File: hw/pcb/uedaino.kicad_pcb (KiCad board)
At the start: 2 copper layers, 6 parts, among them IC1 ATMEGA328P-A, SW1 SW_PUSH

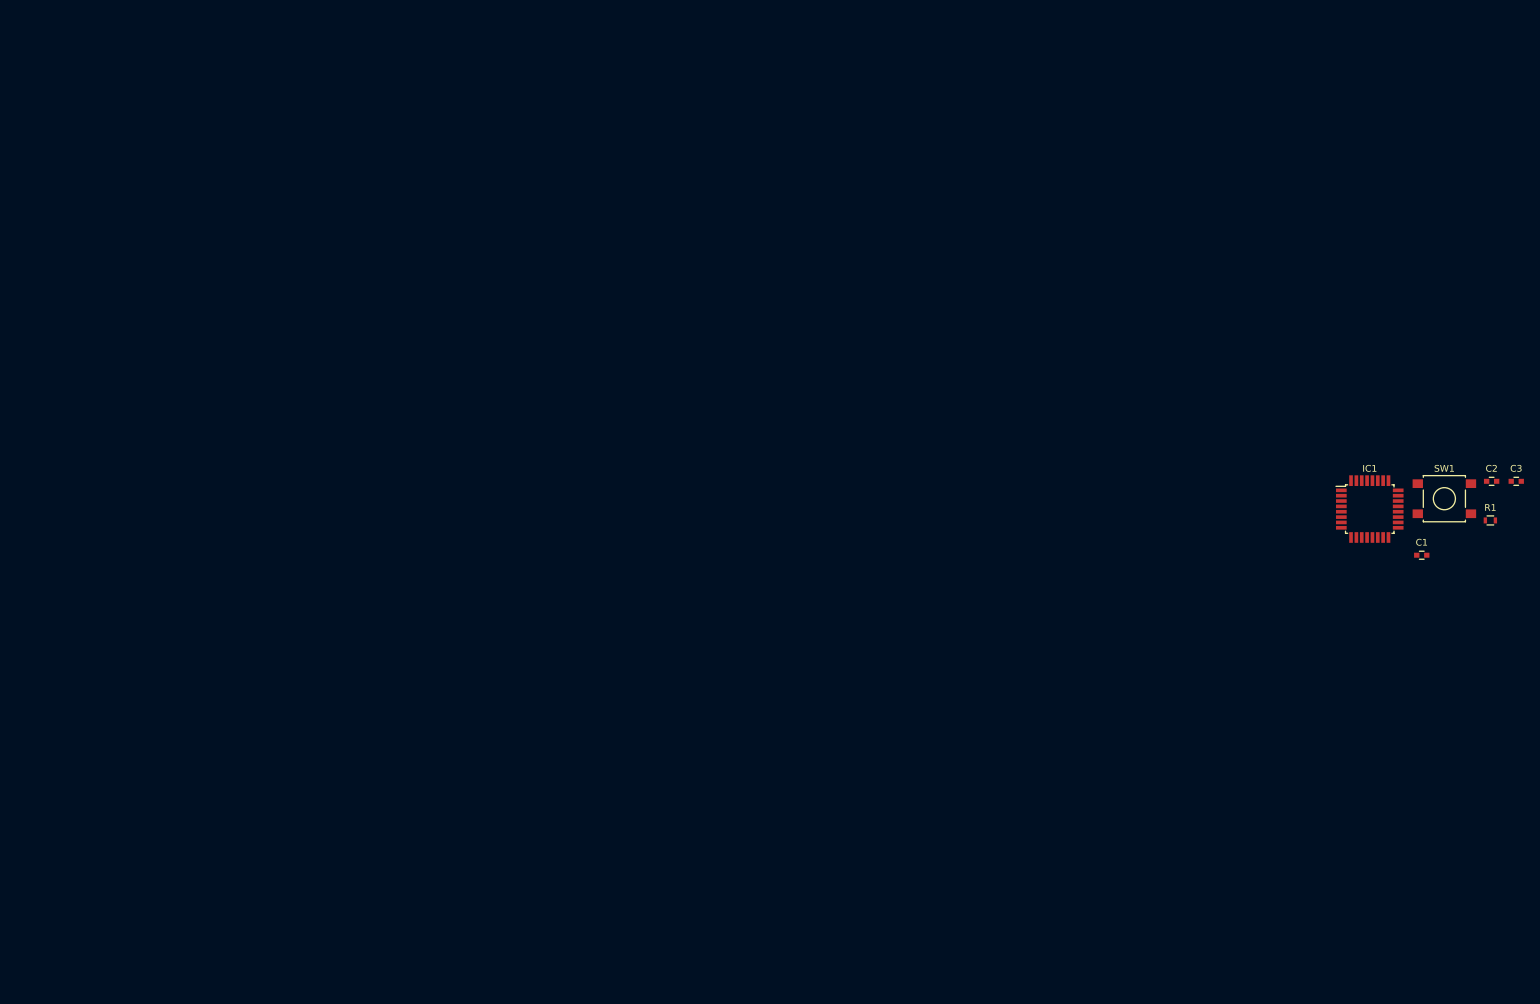
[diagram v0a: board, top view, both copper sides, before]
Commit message: Add functions
Add power circuit.
Add Capacitive Touch Sensor circuit.
Add pin header.
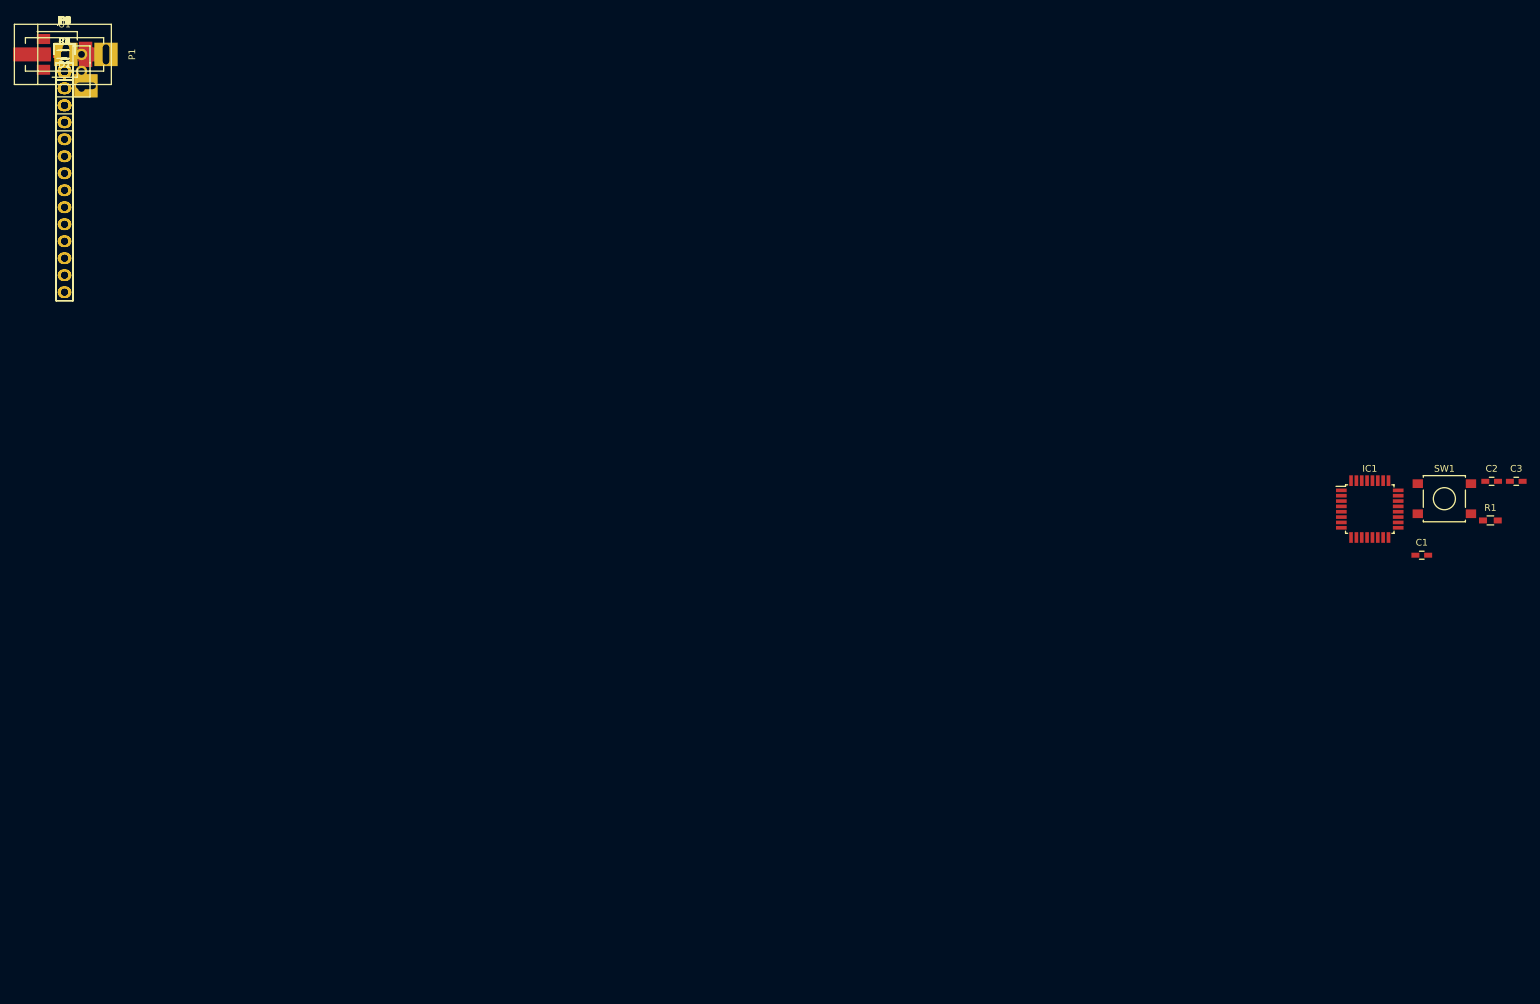
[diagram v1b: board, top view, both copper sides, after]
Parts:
- added C4, C5: 10uF, Capacitors_SMD:C_0603_HandSoldering, F.Cu at (0.00, 0.00)
- added C6, C7: 22uF, Capacitors_SMD:C_0603_HandSoldering, F.Cu at (0.00, 0.00)
- added D1: LED_+5V, Diodes_SMD:D_0603, F.Cu at (0.00, 0.00)
- added D2: LED_+3V3, Diodes_SMD:D_0603, F.Cu at (0.00, 0.00)
- added JP1, JP2, JP3, JP4, JP5, JP6, JP7, JP8, JP9: Jumper_NC_Small, Pin_Headers:Pin_Header_Straight_1x02, F.Cu at (0.00, 0.00)
- added P1: CN_PWR, Connect:BARREL_JACK, F.Cu at (0.00, 0.00)
- added P2: CN_UART, Pin_Headers:Pin_Header_Straight_1x05, F.Cu at (0.00, 0.00)
- added P3: CN_HEADER1, Pin_Headers:Pin_Header_Straight_1x15, F.Cu at (0.00, 0.00)
- added P4: CN_I2C, Pin_Headers:Pin_Header_Straight_1x04, F.Cu at (0.00, 0.00)
- added P5: CN_HEADER2, Pin_Headers:Pin_Header_Straight_1x15, F.Cu at (0.00, 0.00)
- added P6: CN_ICSP, Pin_Headers:Pin_Header_Straight_2x03, F.Cu at (0.00, 0.00)
- added R2: 10M, Resistors_SMD:R_0603_HandSoldering, F.Cu at (0.00, 0.00)
- added R3, R4: 1K, Resistors_SMD:R_0603_HandSoldering, F.Cu at (0.00, 0.00)
- added R5, R6: 4.7K, Resistors_SMD:R_0603_HandSoldering, F.Cu at (0.00, 0.00)
- added U1: AP1117, TO_SOT_Packages_SMD:SOT-223, F.Cu at (0.00, 0.00)
- added Y1: 16MHz, Crystals:Crystal_HC49-SD_SMD, F.Cu at (0.00, 0.00)
- C1, C2, C3: footprint Capacitors_SMD:C_0603 -> Capacitors_SMD:C_0603_HandSoldering
- R1: footprint Resistors_SMD:R_0603 -> Resistors_SMD:R_0603_HandSoldering
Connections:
- C3 pad 1: (no net) -> /DTR
- IC1 pad 1: (no net) -> /D3
- IC1 pad 10: (no net) -> /D6
- IC1 pad 11: (no net) -> /D7
- IC1 pad 12: (no net) -> /D8
- IC1 pad 13: (no net) -> /D9
- IC1 pad 14: (no net) -> /D10
- IC1 pad 15: (no net) -> /D11
- IC1 pad 16: (no net) -> /D12
- IC1 pad 17: (no net) -> /D13
- IC1 pad 19: (no net) -> /A6
- IC1 pad 2: (no net) -> /D4
- IC1 pad 22: (no net) -> /A7
- IC1 pad 23: (no net) -> /A0
- IC1 pad 24: (no net) -> /A1
- IC1 pad 25: (no net) -> /A2
- IC1 pad 26: (no net) -> /A3
- IC1 pad 27: (no net) -> /A4/SDA
- IC1 pad 28: (no net) -> /A5/SCL
- IC1 pad 30: (no net) -> /RXD
- IC1 pad 31: (no net) -> /TXD
- IC1 pad 32: (no net) -> /D2
- IC1 pad 7: (no net) -> /XT1
- IC1 pad 8: (no net) -> /XT2
- IC1 pad 9: (no net) -> /D5
- R1 pad 1: (no net) -> +5V

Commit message: Add PCB Design
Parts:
- removed D2: LED_+3V3, Diodes_SMD:D_0603
- removed JP7, JP8, JP9: Jumper_NC_Small, Pin_Headers:Pin_Header_Straight_1x02
- removed R6: 4.7K, Resistors_SMD:R_0603_HandSoldering
- added U2: WS2812B, UeduinoLib:WS2812B, F.Cu at (154.6, 93.3)
- C3: value 0.1u -> 22uF
- C4: value 10uF -> 22uF
- C6: value 22uF -> 10uF
- C7: value 22uF -> 0.1u
- JP1: value Jumper_NC_Small -> J_CAP1; footprint Pin_Headers:Pin_Header_Straight_1x02 -> UeduinoLib:JP_CAP
- JP2: value Jumper_NC_Small -> J_CAP2; footprint Pin_Headers:Pin_Header_Straight_1x02 -> UeduinoLib:JP_CAP
- JP3: value Jumper_NC_Small -> J_CAP3; footprint Pin_Headers:Pin_Header_Straight_1x02 -> UeduinoLib:JP_CAP
- JP4: value Jumper_NC_Small -> J_CAP4; footprint Pin_Headers:Pin_Header_Straight_1x02 -> UeduinoLib:JP_CAP
- JP5: value Jumper_NC_Small -> J_CAP5; footprint Pin_Headers:Pin_Header_Straight_1x02 -> UeduinoLib:JP_CAP
- JP6: value Jumper_NC_Small -> J_CAP6; footprint Pin_Headers:Pin_Header_Straight_1x02 -> UeduinoLib:JP_CAP
- P1: value CN_PWR -> USB_OTG; footprint Connect:BARREL_JACK -> Connectors:USB_Micro-B_10103594-0001LF
- P2: value CN_UART -> CN_POWER; footprint Pin_Headers:Pin_Header_Straight_1x05 -> Socket_Strips:Socket_Strip_Straight_1x08
- P3: value CN_HEADER1 -> CN_J1; footprint Pin_Headers:Pin_Header_Straight_1x15 -> Socket_Strips:Socket_Strip_Straight_1x06
- P4: value CN_I2C -> CN_ICSP; footprint Pin_Headers:Pin_Header_Straight_1x04 -> Socket_Strips:Socket_Strip_Straight_2x03
- P5: value CN_HEADER2 -> CONN_01X10; footprint Pin_Headers:Pin_Header_Straight_1x15 -> Socket_Strips:Socket_Strip_Straight_1x10
- P6: value CN_ICSP -> CONN_01X08; footprint Pin_Headers:Pin_Header_Straight_2x03 -> Socket_Strips:Socket_Strip_Straight_1x08
- R1: value 10K -> 1K
- R2: value 10M -> 10K
- R3: value 1K -> 10M
- R4: value 1K -> 3.3K
- R5: value 4.7K -> 3.3K
- Y1: footprint Crystals:Crystal_HC49-SD_SMD -> Crystals:Crystal_SMD_5032_2Pads
- moved P6 192.8 mm to (161.3, 105.6), turned to 270 degrees
- moved JP6 191.6 mm to (149.8, 119.6)
- moved JP3 185.0 mm to (149.8, 108.6)
- moved JP5 182.6 mm to (138.0, 119.6)
- moved P5 179.6 mm to (161.3, 79.0), turned to 270 degrees
- moved C4 176.8 mm to (145.6, 100.3), turned to 270 degrees
- moved JP2 175.8 mm to (138.1, 108.7)
- moved P4 173.8 mm to (151.4, 85.2)
- moved JP4 172.9 mm to (125.7, 118.7)
- moved Y1 172.3 mm to (140.0, 100.5), turned to 180 degrees
- moved R4 172.3 mm to (152.6, 79.9)
- moved R5 171.1 mm to (152.7, 77.2)
- moved JP1 166.8 mm to (126.5, 108.7)
- moved C6 166.2 mm to (146.6, 78.2), turned to 90 degrees
- moved U1 160.5 mm to (139.4, 79.6)
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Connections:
- C2 pad 1: Net-(C2-Pad1) -> /AREF
- C3 pad 1: /DTR -> /XT1
- C3 pad 2: /RESET -> GND
- C4 pad 1: +5V -> GND
- C4 pad 2: GND -> /XT2
- C5 pad 1: +3V3 -> +5V
- C6 pad 1: /XT1 -> +3V3
- C7 pad 1: GND -> /DTR
- C7 pad 2: /XT2 -> /RESET
- IC1 pad 15: /D11 -> /D11/MOSI
- IC1 pad 16: /D12 -> /D12/MISO
- IC1 pad 17: /D13 -> /D13/SCK
- IC1 pad 19: /A6 -> (no net)
- IC1 pad 20: Net-(C2-Pad1) -> /AREF
- IC1 pad 22: /A7 -> (no net)
- JP1 pad 1: /D13 -> /D9
- JP2 pad 1: Net-(JP2-Pad1) -> /D8
- JP2 pad 2: /D12 -> Net-(JP1-Pad2)
- JP3 pad 1: Net-(JP2-Pad1) -> /D7
- JP3 pad 2: /D11 -> Net-(JP1-Pad2)
- JP4 pad 1: Net-(JP2-Pad1) -> /D6
- JP4 pad 2: /D10 -> Net-(JP1-Pad2)
- JP5 pad 1: Net-(JP2-Pad1) -> /D5
- JP5 pad 2: /D9 -> Net-(JP1-Pad2)
- JP6 pad 1: Net-(JP2-Pad1) -> /D4
- JP6 pad 2: /D8 -> Net-(JP1-Pad2)
- P1 pad 1: (no net) -> +5V
- P1 pad 2: GND -> (no net)
- P2 pad 1: /RXD -> /DTR
- P2 pad 2: /TXD -> +5V
- P2 pad 3: (no net) -> /RESET
- P2 pad 4: GND -> +3V3
- P2 pad 5: /DTR -> +5V
- P3 pad 1: /TXD -> /A0
- P3 pad 2: /RXD -> /A1
- P3 pad 3: /RESET -> /A2
- P3 pad 4: GND -> /A3
- P3 pad 5: /D2 -> /A4/SDA
- P3 pad 6: /D3 -> /A5/SCL
- P4 pad 1: +3V3 -> /D12/MISO
- P4 pad 2: Net-(JP8-Pad2) -> +5V
- P4 pad 3: Net-(JP9-Pad1) -> /D13/SCK
- P4 pad 4: GND -> /D11/MOSI
- P5 pad 1: (no net) -> /A5/SCL
- P5 pad 10: /A2 -> /D8
- P5 pad 2: GND -> /A4/SDA
- P5 pad 3: /RESET -> /AREF
- P5 pad 4: +5V -> GND
- P5 pad 5: /A7 -> /D13/SCK
- P5 pad 6: /A6 -> /D12/MISO
- P5 pad 7: /A5/SCL -> /D11/MOSI
- P5 pad 8: /A4/SDA -> /D10
- P5 pad 9: /A3 -> /D9
- P6 pad 1: /D12 -> /D7
- P6 pad 2: +5V -> /D6
- P6 pad 3: /D13 -> /D5
- P6 pad 4: /D11 -> /D4
- P6 pad 5: /RESET -> /D3
- P6 pad 6: GND -> /D2
- R1 pad 1: +5V -> Net-(D1-Pad1)
- R1 pad 2: /RESET -> GND
- R2 pad 1: Net-(JP1-Pad2) -> +5V
- R2 pad 2: Net-(JP2-Pad1) -> /RESET
- R3 pad 1: Net-(D1-Pad1) -> /D10
- R3 pad 2: GND -> Net-(JP1-Pad2)
- R4 pad 1: Net-(D2-Pad1) -> +3V3
- R4 pad 2: GND -> /A4/SDA
- R5 pad 2: Net-(JP9-Pad1) -> /A5/SCL
- U1 pad 4: (no net) -> +3V3
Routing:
- net GND: track 0.00 -> 170.3 mm, vias 0 -> 5
- net +5V: track 0.00 -> 105.8 mm, vias 0 -> 6
- net /A5/SCL: track 0.00 -> 87.4 mm, vias 0 -> 4
- net /A4/SDA: track 0.00 -> 81.6 mm, vias 0 -> 3
- net /RESET: track 0.00 -> 63.4 mm, vias 0 -> 2
- net /D2: track 0.00 -> 53.4 mm, vias 0 -> 3
- net /D10: track 0.00 -> 50.8 mm, vias 0 -> 2
- net +3V3: track 0.00 -> 50.3 mm, vias 0 -> 2
- net /D3: track 0.00 -> 47.6 mm, vias 0 -> 1
- net /D4: track 0.00 -> 45.6 mm, vias 0 -> 1
- net /D13/SCK: track 0.00 -> 43.3 mm, vias 0 -> 1
- net /A1: track 0.00 -> 41.6 mm, vias 0 -> 1
- net /A3: track 0.00 -> 41.5 mm, vias 0 -> 1
- net /A2: track 0.00 -> 41.1 mm, vias 0 -> 1
- net /A0: track 0.00 -> 40.9 mm, vias 0 -> 1
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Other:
- board outline added: 50 x 50 mm
- net class Power added: clearance 0.2, trace_width 1, via_dia 0.6, via_drill 0.4

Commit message: Fix layout
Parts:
- moved JP4 13.8 mm to (126.0, 132.5)
- moved JP6 12.9 mm to (150.0, 132.5)
- moved JP5 12.9 mm to (138.0, 132.5)
- moved JP3 11.4 mm to (150.0, 120.0)
- moved JP1 11.3 mm to (126.5, 120.0)
- moved JP2 11.3 mm to (138.1, 120.0)
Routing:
- net Net-(JP1-Pad2): track 2.23 -> 87.9 mm
- net /RXD: track 0.00 -> 54.6 mm, vias 0 -> 4
- net /D6: track 30.6 -> 84.2 mm, vias 1 -> 2
- net /TXD: track 0.00 -> 48.5 mm, vias 0 -> 3
- net /D9: track 23.7 -> 66.8 mm, vias 1 -> 5
- net /D5: track 31.0 -> 67.4 mm, vias 1 -> 5
- net /D8: track 24.8 -> 54.8 mm, vias 1 -> 5
- net /D4: track 45.6 -> 67.2 mm, vias 1 -> 2
- net /D7: track 27.6 -> 49.3 mm, vias 1 -> 5
- net /D2: track 53.4 -> 50.6 mm
- net /D3: track 47.6 -> 44.8 mm
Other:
- board size 50 x 50 mm -> 50 x 65 mm

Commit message: Add silk
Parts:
- added G***: LOGO, silk:fabkominka_logo, B.Cu at (138.1, 108.0)
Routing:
- net (no net): vias 4 -> 3
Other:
- board text added: "Uedaino"
- board text added: "v1.0"

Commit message: Add ground fill
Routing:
- added copper zone on B.Cu, net GND
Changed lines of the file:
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@@
     (links 0)
     (no_connects 3)
-    (area 112.949999 74.949999 163.050001 140.050001)
+    (area 112.073199 72.1996 167.465 140.700002)
     (thickness 1.6)
     (drawings 8)
@@
     (visible_elements 7FFFFFFF)
     (pcbplotparams
-      (layerselection 0x00030_80000001)
-      (usegerberextensions false)
+      (layerselection 0x010f0_80000001)
+      (usegerberextensions true)
       (excludeedgelayer true)
       (linewidth 0.100000)
@@
       (outputformat 1)
       (mirror false)
-      (drillshape 1)
+      (drillshape 0)
       (scaleselection 1)
-      (outputdirectory ""))
+      (outputdirectory gerber/))
   )
   (net 0 "")
@@
   (segment (start 123.5632 98.8568) (end 123.4132 98.8568) (width 0.25) (layer F.Cu) (net 30))
   (segment (start 123.4132 98.8568) (end 120.47 101.8) (width 0.25) (layer F.Cu) (net 30))
+  (zone (net 2) (net_name GND) (layer B.Cu) (hatch edge 0.508)
+    (connect_pads (clearance 0.508))
+    (min_thickness 0.254)
+    (fill yes (arc_segments 16) (thermal_gap 0.508) (thermal_bridge_width 0.508))
+    (polygon
+      (pts
+        (xy 113.7 75.8) (xy 113.5 109.1) (xy 162.8 109.5) (xy 162.4 75.5) (xy 113.6 75.9)
+      )
+    )
+  )
 )
